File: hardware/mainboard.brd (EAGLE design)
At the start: 125 x 75 mm, 42 parts, among them IC1 24LC512P

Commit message: extio.brd, mainboard.brd, gate433.lib
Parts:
- removed IOEXT1: (no value), gate433:1X04
- added EXTIO1: (no value), gate433:1X04
- R1, R2, R3, R4, R5, R6, R7, R8: device resistor:0204/7 -> resistor:R0603
- moved C6 62.5 mm to (67.8, 11.4), turned to 270 degrees
- moved EXT 60.6 mm to (60.7, 15.7), turned to 90 degrees
- moved LCD 58.3 mm to (80.8, 15.7), turned to 90 degrees
- moved U$2 40.0 mm to (80.0, 5.00)
- moved U$3 40.0 mm to (80.0, 70.0)
- moved C9 25.7 mm to (75.2, 11.4)
- moved RF 23.0 mm to (73.9, 48.8), turned to 90 degrees
- moved C4 17.8 mm to (66.5, 16.3)
- moved IC1 14.7 mm to (60.2, 24.1)
- moved CLOCK 14.7 mm to (70.4, 38.1)
- moved C5 14.7 mm to (65.3, 43.4), turned to 180 degrees
- moved C3 13.4 mm to (80.8, 48.8), turned to 270 degrees
- moved R6 12.2 mm to (15.7, 49.0)
- moved R5 9.57 mm to (15.7, 54.1)
- moved R3 7.28 mm to (15.7, 64.3)
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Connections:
- net +5V: now also EXTIO1.2; no longer IOEXT1.2
- net GND: now also EXTIO1.1; no longer IOEXT1.1
- net SCL: now also EXTIO1.4; no longer IOEXT1.4
- net SDA: now also EXTIO1.3; no longer IOEXT1.3
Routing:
- net SDA: track 113.5 -> 78.4 mm, vias 2 -> 0
- net SCL: track 103.9 -> 75.5 mm, vias 1 -> 0
- net N$33: track 68.2 -> 43.5 mm
- net +5V: track 266.7 -> 245.1 mm, vias 2 -> 3
- net N$40: track 17.1 -> 4.74 mm
- net N$3: track 15.0 -> 4.74 mm
- net GNDI5: track 27.2 -> 17.5 mm
- net N$19: track 5.92 -> 14.9 mm
- net N$39: track 12.6 -> 4.74 mm
- net N$2: track 6.03 -> 13.6 mm
- net GNDI1: track 23.7 -> 17.7 mm
- net GNDI6: track 23.1 -> 18.5 mm
- net N$37: track 16.8 -> 12.5 mm
- net N$36: track 16.9 -> 12.8 mm
- net N$41: track 7.76 -> 4.74 mm
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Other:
- board size 125 x 75 mm -> 85 x 75 mm

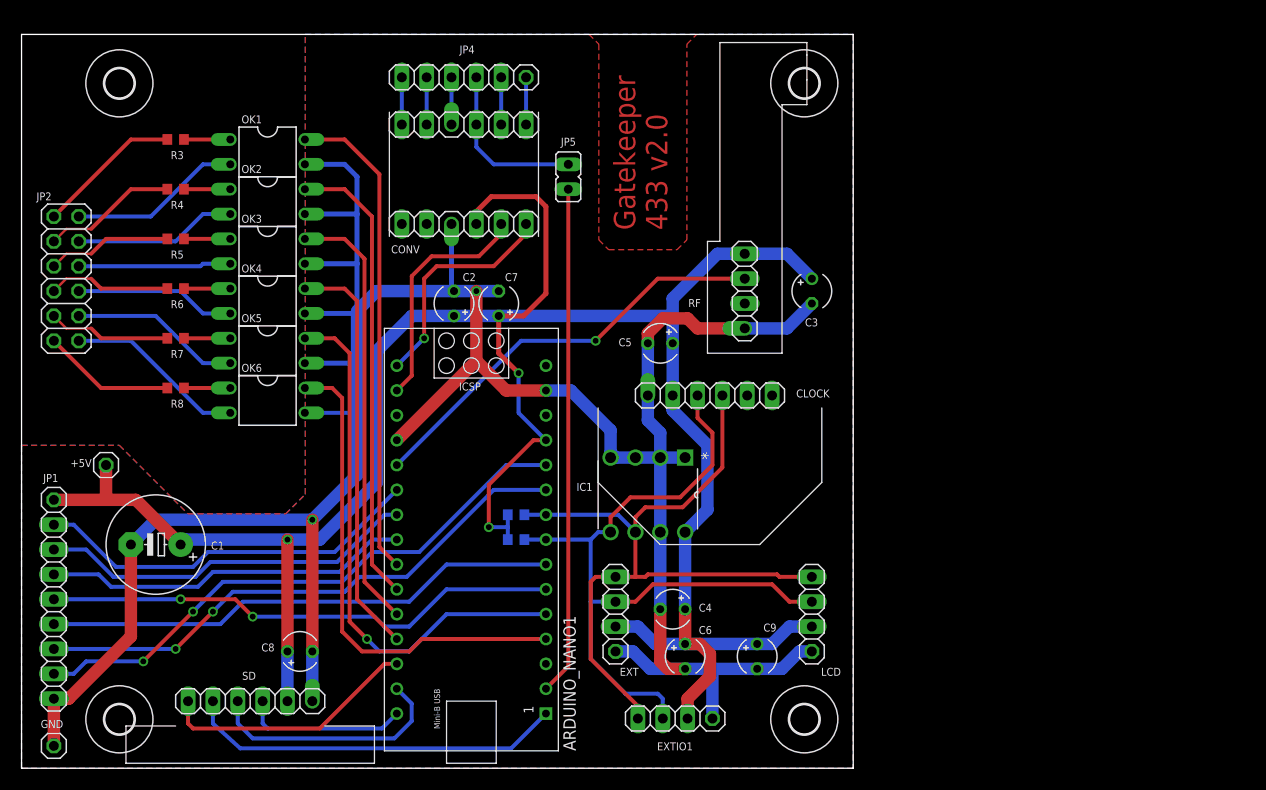
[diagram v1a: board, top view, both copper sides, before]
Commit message: mainboard SMD update
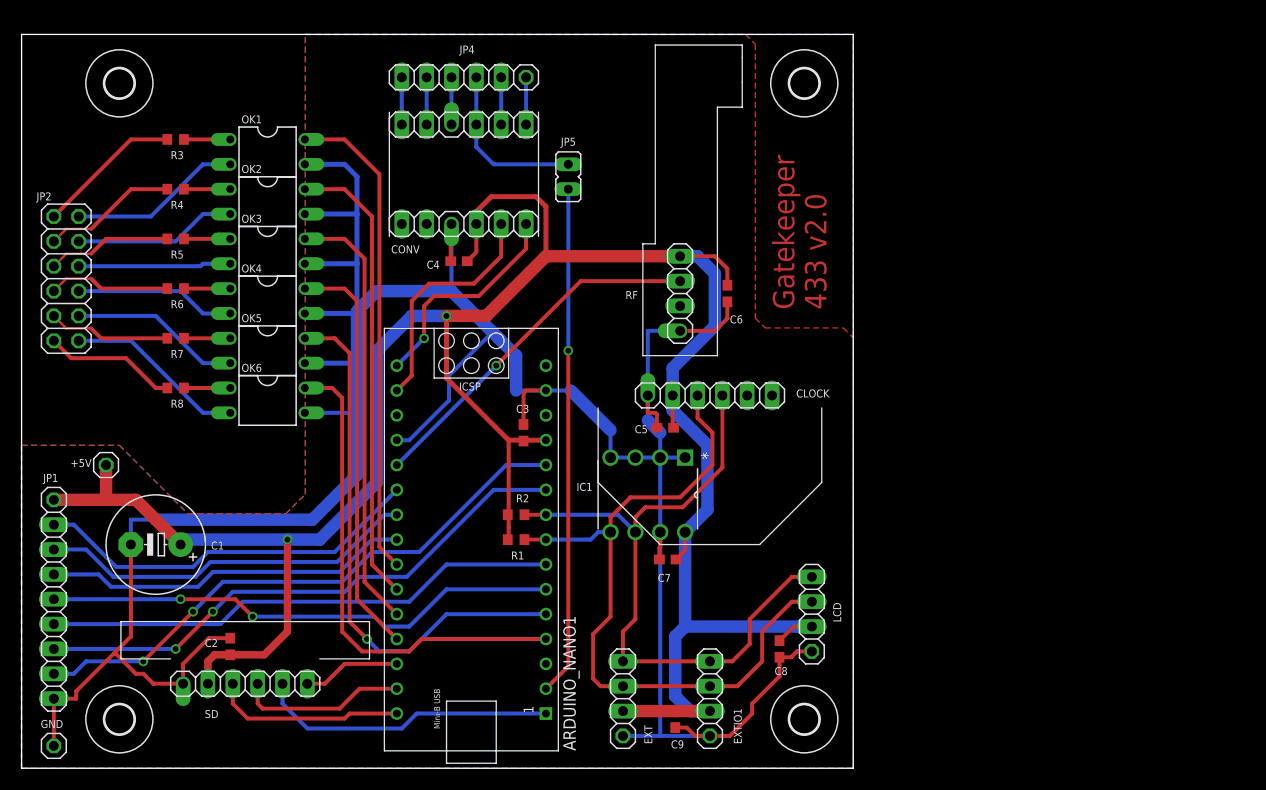
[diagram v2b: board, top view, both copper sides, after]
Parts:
- C2: value 10uF/16V -> 1uF; device resistor:TT2D4 -> resistor:C0603
- C3, C4, C5, C6, C7, C9: device resistor:TT2D4 -> resistor:C0603
- C8: value 100nF -> 1uF; device resistor:TT2D4 -> resistor:C0603
- moved C8 49.0 mm to (77.5, 12.2), turned to 270 degrees
- moved C2 41.8 mm to (21.3, 12.4)
- moved C4 41.7 mm to (44.7, 51.8)
- moved C6 37.3 mm to (72.1, 48.5)
- moved C3 32.8 mm to (51.3, 34.3), turned to 90 degrees
- moved C7 31.3 mm to (66.0, 21.3), turned to 180 degrees
- moved C9 10.6 mm to (66.8, 5.00)
- moved EXT 8.67 mm to (61.5, 7.11)
- moved C5 8.65 mm to (65.8, 34.8)
- moved RF 6.61 mm to (67.3, 48.5)
- moved EXTIO1 4.10 mm to (70.4, 7.11), turned to 90 degrees
- moved SD 1.85 mm to (22.9, 8.64), turned to 0 degrees
- flipped R1 to the top, turned to 180 degrees
- flipped R2 to the top, turned to 180 degrees
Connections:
- net +5V: now also C2.1, C3.1, C4.1, C5.1, C6.1, C7.1, C8.1, C9.1; no longer C2.+, C3.+, C4.+, C5.+, C6.+, C7.+, C8.+, C9.+
- net GND: now also C2.2, C3.2, C4.2, C5.2, C6.2, C7.2, C8.2, C9.2; no longer C2.-, C3.-, C4.-, C5.-, C6.-, C7.-, C8.-, C9.-
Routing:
- net N$14: track 26.6 -> 9.99 mm
- net GND: track 283.2 -> 297.3 mm, vias 2 -> 0
- net +5V: track 245.1 -> 255.1 mm, vias 3 -> 2
- net N$15: track 38.8 -> 30.6 mm
- net N$16: track 25.4 -> 17.3 mm
- net N$33: track 43.5 -> 36.7 mm
- net SCL: track 75.5 -> 70.1 mm
- net SDA: track 78.4 -> 74.8 mm
- net N$17: track 16.8 -> 19.6 mm
- net N$59: track 23.4 -> 22.6 mm
- net +3V3: vias 0 -> 1

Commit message: extio crop and label change, mainboard label change
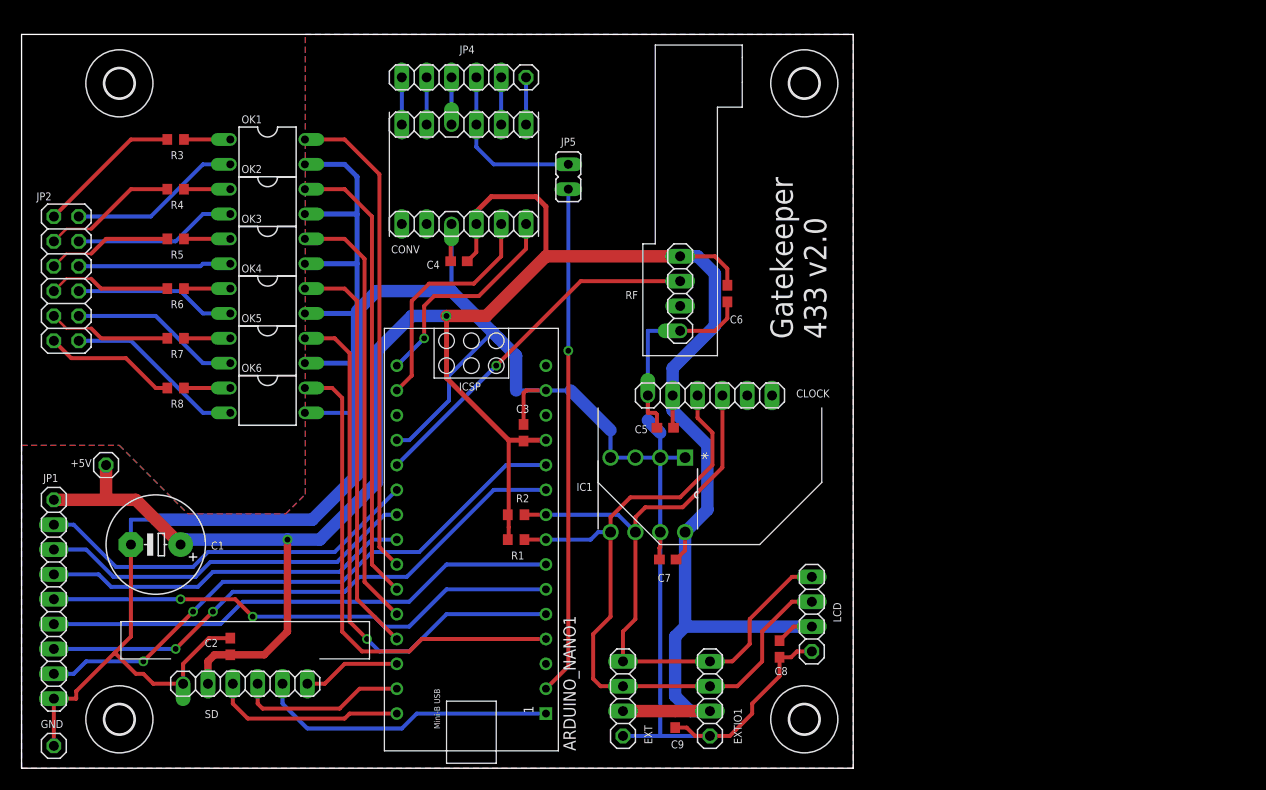
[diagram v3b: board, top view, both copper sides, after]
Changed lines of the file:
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@@
 <layer number="37" name="tTest" color="7" fill="1" visible="yes" active="yes"/>
 <layer number="38" name="bTest" color="7" fill="1" visible="no" active="yes"/>
-<layer number="39" name="tKeepout" color="4" fill="11" visible="yes" active="yes"/>
-<layer number="40" name="bKeepout" color="1" fill="11" visible="yes" active="yes"/>
+<layer number="39" name="tKeepout" color="4" fill="11" visible="no" active="yes"/>
+<layer number="40" name="bKeepout" color="1" fill="11" visible="no" active="yes"/>
 <layer number="41" name="tRestrict" color="4" fill="10" visible="yes" active="yes"/>
 <layer number="42" name="bRestrict" color="1" fill="10" visible="yes" active="yes"/>
@@
 <dimension x1="10" y1="5" x2="0" y2="0" x3="5" y3="-4" textsize="1.778" layer="47" dtype="horizontal"/>
 <dimension x1="80" y1="5" x2="85" y2="0" x3="91" y3="2.5" textsize="1.778" layer="47" dtype="vertical"/>
-<text x="82.256" y="46.872" size="2.1844" layer="1" font="vector" ratio="12" rot="R90">Gatekeeper
+<text x="82.256" y="43.872" size="2.286" layer="21" font="vector" ratio="10" rot="R90">Gatekeeper
 433 v2.0</text>
 </plain>
@@
 </class>
 </classes>
-<designrules name="HuGyártás">
+<designrules name="NYAKARUHAZ_StandardNYAK">
 <description language="de">&lt;b&gt;EAGLE Design Rules&lt;/b&gt;
 &lt;p&gt;
@@
 necessary adjustments and save your customized
 design rules under a new name.</description>
+<description language="hu">&lt;b&gt;EAGLE Tervezési Szabályok&lt;/b&gt;&lt;p&gt;Az alapértelmezett Tervezési Szabályok úgy lettek megállapítva, hogy használhatók legyenek minél többféle alkalmazás megtervezéséhez.A Te általad tervezni kívánt termék más beállításokat követelhet meg,így megkérlek, hogy tedd meg a neked szükséges beállításokat, és mentsd elegy másik néven.</description>
 <param name="layerSetup" value="(1*16)"/>
 <param name="mtCopper" value="0.035mm 0.035mm 0.035mm 0.035mm 0.035mm 0.035mm 0.035mm 0.035mm 0.035mm 0.035mm 0.035mm 0.035mm 0.035mm 0.035mm 0.035mm 0.035mm"/>
 <param name="mtIsolate" value="1.5mm 0.15mm 0.2mm 0.15mm 0.2mm 0.15mm 0.2mm 0.15mm 0.2mm 0.15mm 0.2mm 0.15mm 0.2mm 0.15mm 0.2mm"/>
-<param name="mdWireWire" value="8mil"/>
-<param name="mdWirePad" value="8mil"/>
-<param name="mdWireVia" value="8mil"/>
-<param name="mdPadPad" value="8mil"/>
-<param name="mdPadVia" value="8mil"/>
-<param name="mdViaVia" value="8mil"/>
-<param name="mdSmdPad" value="8mil"/>
-<param name="mdSmdVia" value="8mil"/>
-<param name="mdSmdSmd" value="8mil"/>
+<param name="mdWireWire" value="6mil"/>
+<param name="mdWirePad" value="6mil"/>
+<param name="mdWireVia" value="6mil"/>
+<param name="mdPadPad" value="6mil"/>
+<param name="mdPadVia" value="6mil"/>
+<param name="mdViaVia" value="6mil"/>
+<param name="mdSmdPad" value="6mil"/>
+<param name="mdSmdVia" value="6mil"/>
+<param name="mdSmdSmd" value="6mil"/>
 <param name="mdViaViaSameLayer" value="8mil"/>
 <param name="mnLayersViaInSmd" value="2"/>
-<param name="mdCopperDimension" value="8mil"/>
+<param name="mdCopperDimension" value="20mil"/>
 <param name="mdDrill" value="8mil"/>
 <param name="mdSmdStop" value="0mil"/>
-<param name="msWidth" value="10mil"/>
-<param name="msDrill" value="0.5mm"/>
+<param name="msWidth" value="6mil"/>
+<param name="msDrill" value="12mil"/>
 <param name="msMicroVia" value="9.99mm"/>
 <param name="msBlindViaRatio" value="0.5"/>
@@
 <param name="mlMinCreamFrame" value="0mil"/>
 <param name="mlMaxCreamFrame" value="0mil"/>
-<param name="mlViaStopLimit" value="20mil"/>
+<param name="mlViaStopLimit" value="0mil"/>
 <param name="srRoundness" value="0"/>
 <param name="srMinRoundness" value="0mil"/>
 <param name="srMaxRoundness" value="0mil"/>
-<param name="slThermalIsolate" value="10mil"/>
+<param name="slThermalIsolate" value="6mil"/>
 <param name="slThermalsForVias" value="0"/>
 <param name="dpMaxLengthDifference" value="10mm"/>
@@
 <vertex x="29" y="28"/>
 <vertex x="29" y="75"/>
-<vertex x="74" y="75"/>
-<vertex x="75" y="74"/>
-<vertex x="75" y="46"/>
-<vertex x="76" y="45"/>
-<vertex x="84" y="45"/>
-<vertex x="85" y="44"/>
+<vertex x="85" y="75"/>
 <vertex x="85" y="0"/>
 <vertex x="0" y="0"/>
